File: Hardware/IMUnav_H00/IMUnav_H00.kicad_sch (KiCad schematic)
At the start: 13 parts, among them U11 OLED_I2C, U7 STM32F446VETx

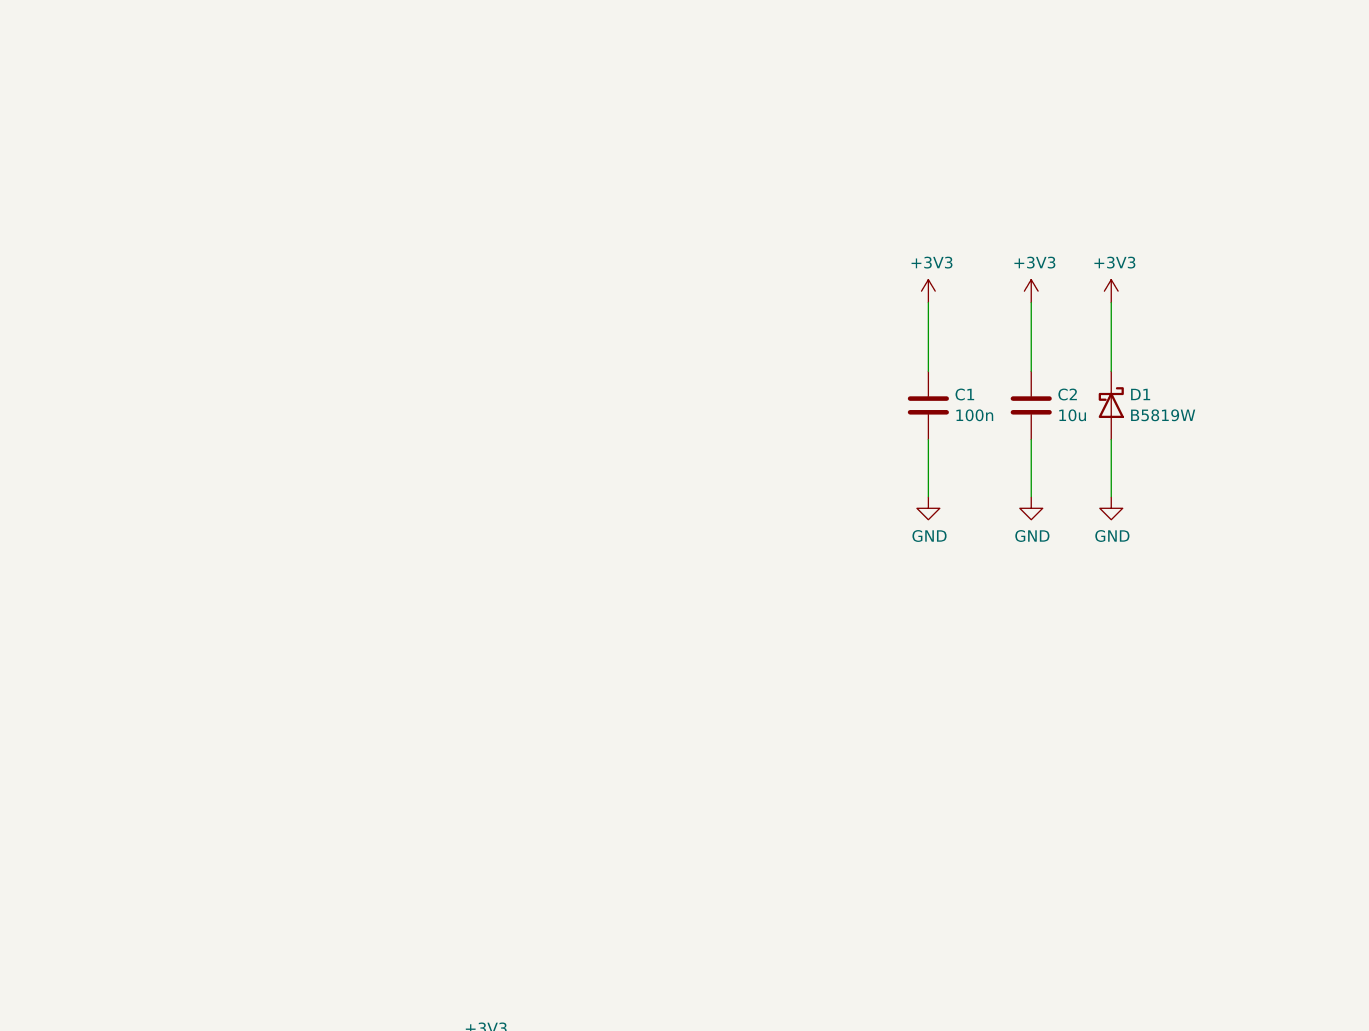
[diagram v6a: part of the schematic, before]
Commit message: Added uSD card, changed ESP module to C3-MINI, changed MCU to STM32F4
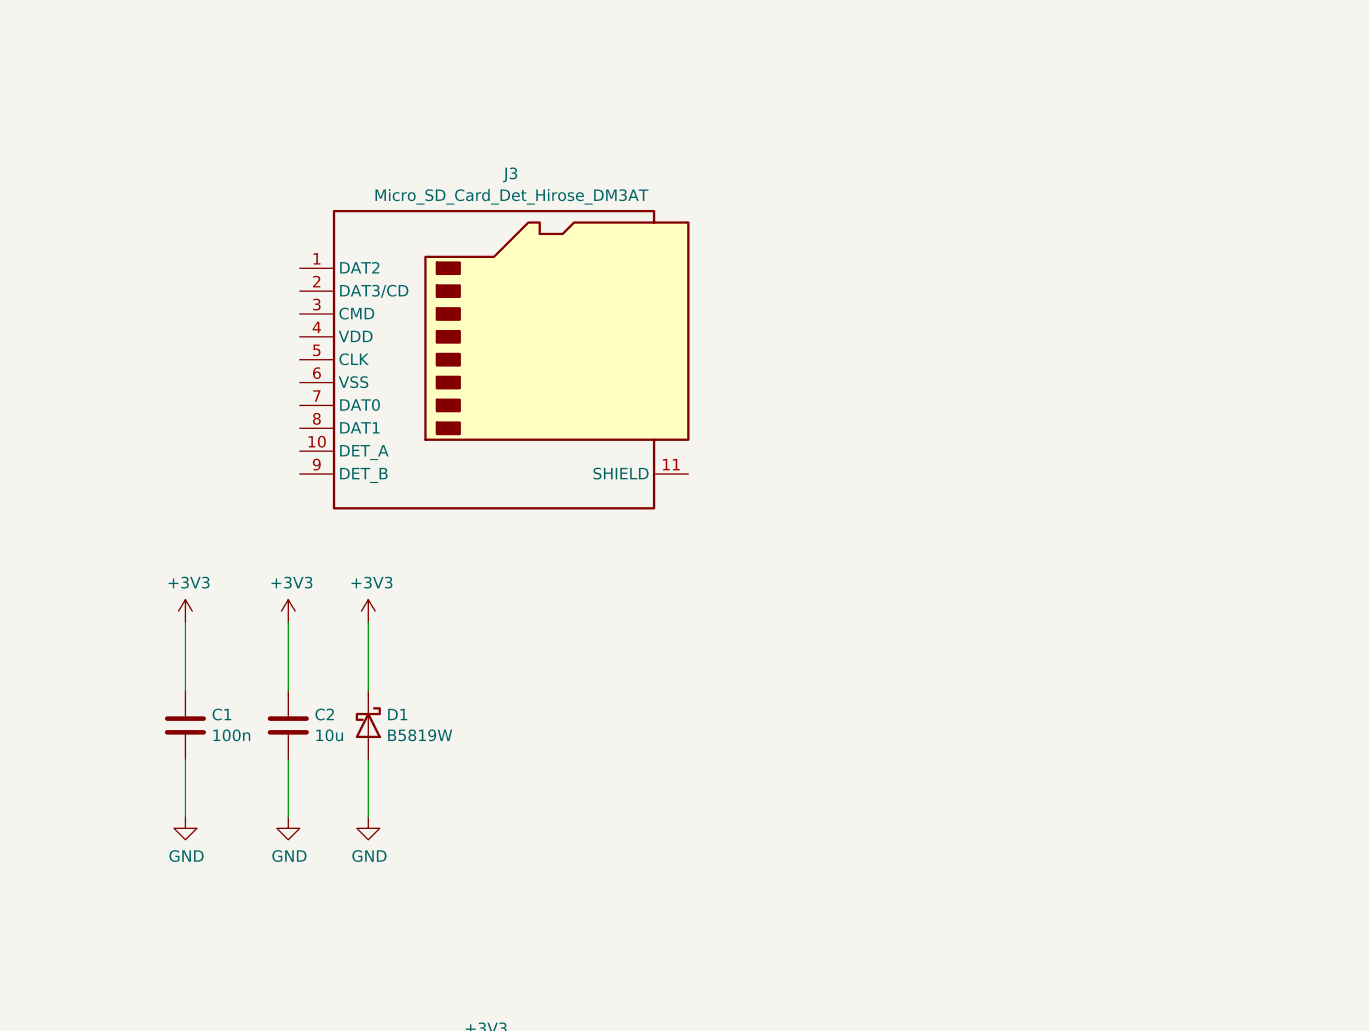
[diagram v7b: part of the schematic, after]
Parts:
- added J3: Micro_SD_Card_Det_Hirose_DM3AT, Connector_Card:microSD_HC_Hirose_DM3AT-SF-PEJM5, symbol Connector:Micro_SD_Card_Det_Hirose_DM3AT
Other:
- moved on the sheet: C1, C2, D1

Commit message: Added sheets for memory and UserInterface
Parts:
- removed C45: 100n, Capacitor_SMD:C_0603_1608Metric, symbol Device:C
- removed D1: B5819W, Diode_SMD:D_SOD-123, symbol Device:D_Schottky
- removed D6: 3V3, Diode_SMD:D_MiniMELF, symbol Device:D_Zener
- removed J3: Micro_SD_Card_Det_Hirose_DM3AT, Connector_Card:microSD_HC_Hirose_DM3AT-SF-PEJM5, symbol Connector:Micro_SD_Card_Det_Hirose_DM3AT
- removed U11: OLED_I2C, IMUnav:Display_128x64_096_I2C, symbol IMUnav:OLED_I2C
- added C63, C64, C65, C66, C67, C68, C69, C70, C71: 100n, Capacitor_SMD:C_0603_1608Metric, symbol Device:C
- added C72, C73: 2u2, Capacitor_SMD:C_0603_1608Metric, symbol Device:C
- added J4: Conn_01x03_Pin, symbol Connector:Conn_01x03_Pin
- added R44 (x5): 10K, Resistor_SMD:R_0603_1608Metric, symbol Device:R
- added SW2: SW_SPST, Button_Switch_THT:SW_PUSH_6mm_H13mm, symbol Switch:SW_SPST
- added SWD: Conn_01x06_Pin, Connector_PinHeader_2.54mm:PinHeader_1x06_P2.54mm_Vertical, symbol Connector:Conn_01x06_Pin
- added X1: SX5M24.000M20F30TNN, IMUnav:OSC_ECS-3963-250-BN-TR, symbol IMUnav:ECS-5032MV
- C2: value 10u -> 100n; footprint Capacitor_SMD:C_0805_2012Metric -> Capacitor_SMD:C_0603_1608Metric; LCSC C15850 -> C14663
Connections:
- net +3V3: now also U7.100 (VDD), U7.11 (VDD), U7.19 (VDD), U7.21 (VREF+), U7.22 (VDDA), U7.28 (VDD), U7.50 (VDD), U7.75 (VDD), C63.1, C64.1, C65.1, C66.1, C67.1, C68.1, R44.1, R44.1, R44.1, SW2.2 (B), SWD.1 (Pin_1), X1.1 (Tri-State), X1.4 (Vcc)
- net GND: now also U7.10 (VSS), U7.20 (VSSA), U7.27 (VSS), U7.49 (VSS), U7.74 (VSS), U7.99 (VSS), C63.2, C64.2, C65.2, C66.2, C67.2, C68.2, C69.2, C70.2, C71.2, C72.2, C73.2, J4.3 (Pin_3), R44.2, R44.2, SWD.3 (Pin_3), X1.2 (GND)
- net GPS/GPS_BCKP_POWER: now also U7.6 (VBAT), C71.1
- net at U7.12 (PH0): now also X1.3 (OUT)
- net SWD_NRST: now reaches U7.14 (NRST)
- net SWD_NRST: now also C69.1, R44.2, SWD.5 (Pin_5)
- net BOOT1: now reaches U7.37 (PB2)
- net BOOT1: now also R44.1
- net at U7.48 (VCAP_1): now also C73.1
- net OLED_SDA: now reaches U7.60 (PD13)
- net OLED_SDA: now also J4.1 (Pin_1), R44.2
- net OLED_SCL: now reaches U7.61 (PD14)
- net OLED_SCL: now also J4.2 (Pin_2), R44.2
- net SWD_SWIO: now reaches U7.72 (PA13)
- net SWD_SWIO: now also SWD.4 (Pin_4)
- net at U7.73 (VCAP_2): now also C72.1
- net SWD_CLK: now reaches U7.76 (PA14)
- net SWD_CLK: now also SWD.2 (Pin_2)
- net SWD_SWO: now reaches U7.89 (PB3)
- net SWD_SWO: now also SWD.6 (Pin_6)
- net at U7.94 (BOOT0): now also C70.1, R44.1, SW2.1 (A)
- no-connect marks 2 -> 3
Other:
- added sheet Memory (Memory.kicad_sch)
- added sheet User (User.kicad_sch)
- note added: "HW notes: Done - consider different module / chip package for ESP32 Used different approach - Consider high-side switches for peripherals (at leaset those that have high power consumption on reset/shutdown) Done - Add battery and switch Done - Add 5V and BAT voltage sensing Used different approach - Add diodes/mosfets for powering DC/DC converter from USB/Battery automatically Done - 100kHz SMBUS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"
- note added: "Koupit na TME: SMA konektor 901-143: 901-143-6RFX plochý kabel 1mm: DS1052-01-16NA2015 Konektor 2x8 1mm na desku THT: 57102-F08-08ULF Konektor 2x8 1mm krimpovací na kabel: T826116A101CEU Tlačítka?"
- note removed: "HW notes: consider different module / chip package for ESP32 Consider high-side switches for peripherals (at leaset those that have high power consumption on reset/shutdown) Done - Add battery and switch Done - Add 5V and BAT voltage sensing Add diodes/mosfets for powering DC/DC converter from USB/Battery automatically Done - 100kHz SMBUS - check max i2c speed of usb hub, so it does not collide w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"
- note removed: "Koupit na TME: SMA konektor 901-143: 901-143-6RFX plochý kabel 1mm: DS1052-01-16NA2015 Konektor 2x8 1mm na desku THT: 57102-F08-08ULF Konektor 2x8 1mm krimpovací na kabel: T826116A101CEU"
- moved on the sheet: C1, H1, H2, H3, H4, U7
